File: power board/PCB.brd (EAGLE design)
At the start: 102.5 x 81.3 mm, 74 parts, among them IC1 MCP2515-E/ST, Q1 BUZ10, Q2 QUARZ5, U1 INA209_PW_16, U2 UCC2837_D_8, U3 AD5252BRU10, U5 MSP430FR5739_DA_38, U6 SN65HVD235_D_8

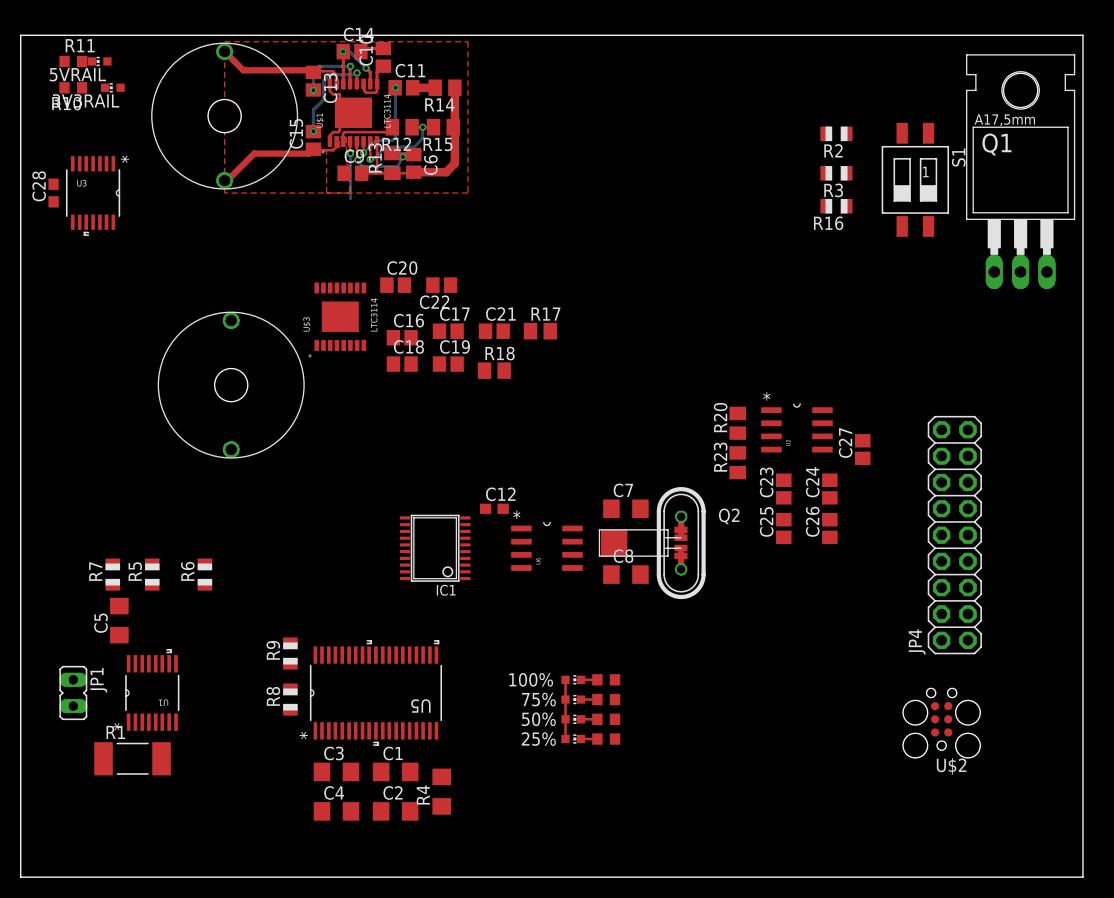
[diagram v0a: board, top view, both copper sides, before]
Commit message: PCB layout of power rails
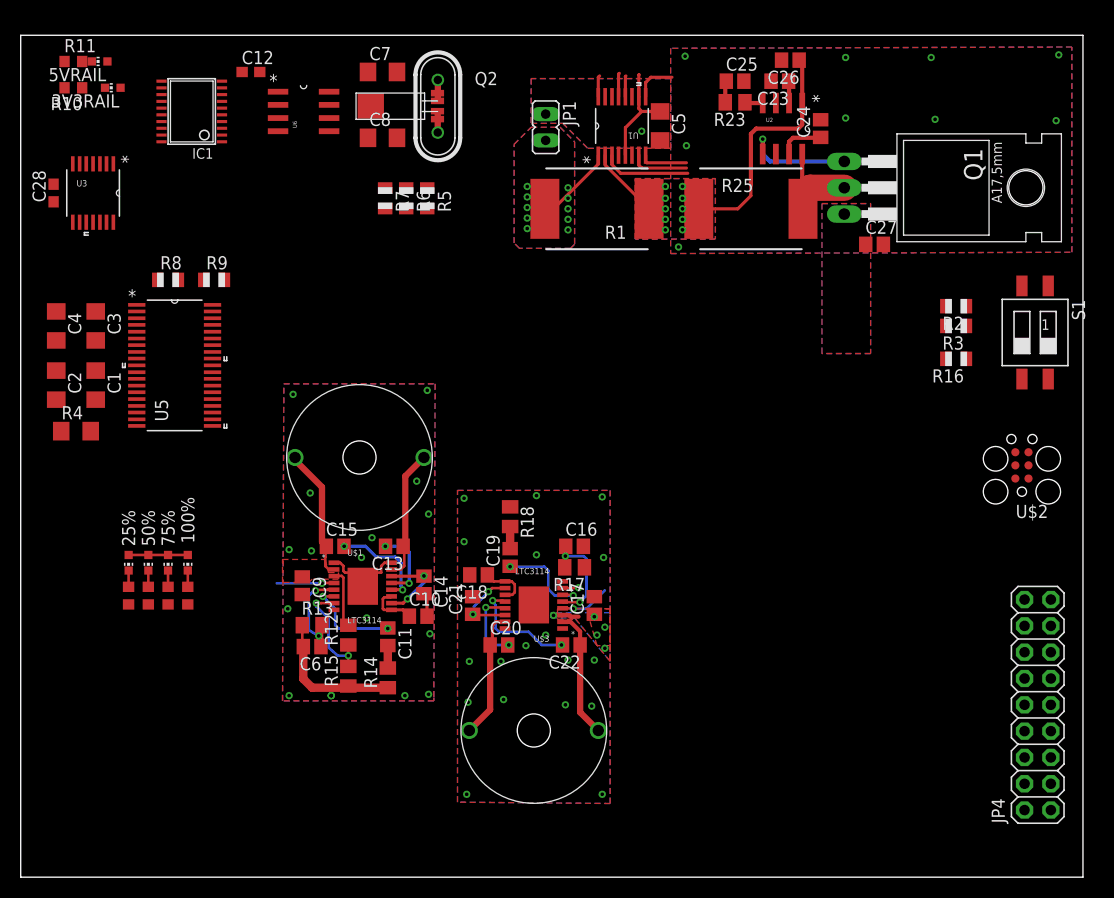
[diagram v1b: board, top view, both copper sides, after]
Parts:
- removed R20: .02, adafruit:M0805
- added R25: (no value), resistor-shunt:SMR
- R1: device resistor:R2512 -> resistor-shunt:SMR
- moved JP1 71.1 mm to (50.7, 72.4)
- moved U1 71.1 mm to (58.0, 72.5)
- moved C5 70.7 mm to (61.7, 72.5), turned to 270 degrees
- moved R1 69.5 mm to (55.6, 64.5), turned to 180 degrees
- moved R14 57.2 mm to (35.4, 19.2), turned to 90 degrees
- moved C4 54.1 mm to (3.43, 53.2), turned to 270 degrees
- moved C10 54.0 mm to (38.4, 25.2), turned to 0 degrees
- moved R15 53.8 mm to (31.6, 19.4), turned to 90 degrees
- moved C11 53.0 mm to (35.4, 23.2), turned to 270 degrees
- moved C2 52.6 mm to (3.43, 47.5), turned to 270 degrees
- moved C14 51.9 mm to (38.9, 28.2), turned to 270 degrees
- moved R4 49.6 mm to (5.33, 43.1), turned to 0 degrees
- moved R12 49.3 mm to (31.6, 23.4), turned to 90 degrees
- moved C3 48.9 mm to (7.24, 53.2), turned to 270 degrees
- moved C12 48.3 mm to (22.2, 77.7)
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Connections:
- removed net N$36: C21.1, C26.1, R20.2, U$3.10, U$3.14, U2.1
- net BAT_WARN: now also R5.2
- net GND: now also C10.2, C14.2, C16.2, C18.2, C21.2, C23.2, C24.2, C25.2, C26.2, C27.2, C28.2, C5.2, C6.2, IC1.10, JP1.1, R13.1, R14.1, R15.1, R16.1, R17.1, R18.1, S1.1, U$1.1, U$1.16, U$1.8, U$1.PAD, U$3.1, U$3.16, U$3.8, U$3.PAD, U1.4, U2.3, U3.10, U3.11, U3.13, U3.5, U3.8, U5.3, U6.2
- net GNDA: no longer C10.2, C14.2, C16.2, C18.2, C21.2, C23.2, C24.2, C25.2, C26.2, C27.2, C28.2, C5.2, C6.2, IC1.10, JP1.1, R13.1, R14.1, R15.1, R16.1, R17.1, R18.1, S1.1, U$1.1, U$1.16, U$1.8, U$1.PAD, U$3.1, U$3.16, U$3.8, U$3.PAD, U1.4, U2.3, U3.10, U3.11, U3.13, U3.5, U3.8, U5.3, U6.2
- net N$25: now also R25.1; no longer R20.1
- net VBUS_BYPASS: now also Q1.1, U2.5
- net VBUS_ENABLE: no longer Q1.1, U2.5
- net VCC: now also C21.1, C26.1, R25.2, U$3.10, U$3.14, U2.1
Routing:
- net VCC: track 7.74 -> 45.5 mm, vias 2 -> 14
- net GNDA: track 26.3 -> 0.00 mm
- net GND: track 0.00 -> 20.3 mm, vias 0 -> 45
- net N$12: track 0.00 -> 12.5 mm
- net N$10: track 0.00 -> 12.4 mm
- net VBUS_BYPASS: track 0.00 -> 11.1 mm, vias 0 -> 1
- net N$18: track 0.00 -> 11.0 mm, vias 0 -> 2
- net N$25: track 0.00 -> 10.9 mm
- net N$19: track 0.00 -> 10.4 mm, vias 0 -> 2
- net +3V3: track 11.6 -> 21.9 mm
- net N$22: track 0.00 -> 9.36 mm, vias 0 -> 2
- net TRIGGER_CONVERT: track 0.00 -> 8.58 mm
- net VCC_1: track 0.00 -> 7.91 mm, vias 0 -> 10
- net N$14: track 0.00 -> 7.33 mm, vias 0 -> 2
- net BAT_CRITICAL: track 0.00 -> 5.68 mm
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- added copper zone on layer 1, net +5V
- added copper zone on layer 16, net +5V
- added copper zone on layer 1, net GND
- added copper zone on layer 16, net GND
- added copper zone on layer 1, net VBUS
- added copper zone on layer 16, net VBUS
- added copper zone on layer 1, net VCC
- added copper zone on layer 16, net VCC
- added copper zone on layer 1, net VCC_1
- added copper zone on layer 16, net VCC_1
- removed copper zone on layer 1, net GNDA

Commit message: additional pcb work
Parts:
- removed JP1: (no value), jumper:JP1
- added U$6: MOLEX_15-31-1026, connectors:MOLEX-15-31-1026
- added X1: (no value), con-wago-500:W237-102
- JP4: device adafruit:2X09-BIG -> con-lsta:FE05-2
- moved S1 89.8 mm to (11.6, 77.2), turned to 270 degrees
- moved C4 75.1 mm to (65.3, 10.5), turned to 90 degrees
- moved JP4 74.3 mm to (23.9, 15.6), turned to 0 degrees
- moved R16 73.2 mm to (23.2, 79.4)
- moved 3V3RAIL 73.1 mm to (22.6, 4.45)
- moved 5VRAIL 73.1 mm to (21.3, 6.99)
- moved R10 73.1 mm to (18.8, 4.45)
- moved R11 73.1 mm to (18.8, 6.99)
- moved C3 70.4 mm to (63.2, 10.5), turned to 90 degrees
- moved R2 70.3 mm to (23.5, 77.1)
- moved C2 68.5 mm to (55.8, 3.30), turned to 180 degrees
- moved R3 68.1 mm to (27.1, 78.4), turned to 270 degrees
- moved U$2 62.0 mm to (42.5, 9.53)
- moved C12 57.9 mm to (48.4, 26.0)
- moved U5 56.9 mm to (55.8, 9.91), turned to 270 degrees
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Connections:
- net GND: now also C17.2, U$6.2, X1.2; no longer JP1.1, JP4.12, JP4.14, JP4.16, JP4.18
- net GNDA: no longer C17.2
- net VBUS: now also U$6.1; no longer JP4.11, JP4.13, JP4.15, JP4.17
- net VCC_1: now also X1.1; no longer JP1.2
- net XIN: now also C7.1, Q2.2; no longer C8.1, Q2.1
- net XOUT: now also C8.1, Q2.1; no longer C7.1, Q2.2
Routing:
- net VCC: track 45.5 -> 99.1 mm, vias 14 -> 15
- net +3V3: track 21.9 -> 61.8 mm, vias 0 -> 1
- net N$28: track 0.00 -> 39.6 mm, vias 0 -> 2
- net +5V: track 2.49 -> 31.3 mm, vias 5 -> 4
- net VBUS_ENABLE: track 2.16 -> 30.6 mm
- net GND: track 20.3 -> 47.8 mm, vias 45 -> 47
- net VBUS_BYPASS: track 11.1 -> 35.2 mm
- net BAT_OVERLIM: track 4.60 -> 26.1 mm, vias 0 -> 1
- net BAT_CRITICAL: track 5.68 -> 24.6 mm, vias 0 -> 1
- net TRIGGER_CONVERT: track 8.58 -> 22.8 mm, vias 0 -> 1
- net SCL: track 2.03 -> 15.8 mm
- net BAT_WARN: track 4.12 -> 17.1 mm
- net RX_CAN: track 0.00 -> 12.7 mm
- net SDA: track 2.29 -> 14.7 mm
- net SMBALERT: track 2.06 -> 13.2 mm
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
